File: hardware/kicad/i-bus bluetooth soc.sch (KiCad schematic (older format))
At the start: 35 parts, among them J1 CONN_3, J2 CONN_6, U1 CC2541, U2 TH8080, U3 MC34063, U4 TPS76933, X1 32 MHz

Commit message: Rules check found missing NCs
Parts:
- removed GND: GND, symbol GND
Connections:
- no-connect marks 2 -> 17
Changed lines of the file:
@@
-EESchema Schematic File Version 2  date Mon 17 Feb 2014 12:44:29 PM CST
+EESchema Schematic File Version 2  date Mon 17 Feb 2014 01:35:22 PM CST
 LIBS:power
 LIBS:device
@@
 LIBS:TLV70033
 LIBS:guan
-EELAYER 43  0
+LIBS:i-bus bluetooth soc-cache
+EELAYER 25  0
 EELAYER END
 $Descr A4 11700 8267
@@
 Comment4 ""
 $EndDescr
+NoConn ~ 8800 5000
+NoConn ~ 8800 4900
+NoConn ~ 8800 4800
+NoConn ~ 8800 4500
+NoConn ~ 8800 4400
+NoConn ~ 8800 3100
+NoConn ~ 8800 3000
+NoConn ~ 8800 2700
+NoConn ~ 8800 2600
+NoConn ~ 8800 2500
+NoConn ~ 8800 2400
+NoConn ~ 8800 2000
+NoConn ~ 8800 1900
+NoConn ~ 8800 1600
+NoConn ~ 8800 1500
 Text Label 3250 4850 0    60   ~ 0
 AVDD1,2,4
@@
 DVDD2
 $Comp
-L +3.3V #PWR?
+L +3.3V #+3.3V01
 U 1 1 530255BC
 P 1400 4800
-F 0 "#PWR?" H 1400 4760 30  0001 C CNN
+F 0 "#+3.3V01" H 1400 4760 30  0001 C CNN
 F 1 "+3.3V" H 1400 4910 30  0000 C CNN
 	1    1400 4800
@@
 $EndComp
 $Comp
-L GND #PWR?
+L GND #GND02
 U 1 1 53025587
 P 3600 5350
-F 0 "#PWR?" H 3600 5350 30  0001 C CNN
+F 0 "#GND02" H 3600 5350 30  0001 C CNN
 F 1 "GND" H 3600 5280 30  0001 C CNN
 	1    3600 5350
@@
 $EndComp
 $Comp
-L GND #PWR?
+L GND #GND03
 U 1 1 53025585
 P 3250 5350
-F 0 "#PWR?" H 3250 5350 30  0001 C CNN
+F 0 "#GND03" H 3250 5350 30  0001 C CNN
 F 1 "GND" H 3250 5280 30  0001 C CNN
 	1    3250 5350
@@
 $EndComp
 $Comp
-L GND #PWR?
+L GND #GND04
 U 1 1 53025583
 P 1500 5350
-F 0 "#PWR?" H 1500 5350 30  0001 C CNN
+F 0 "#GND04" H 1500 5350 30  0001 C CNN
 F 1 "GND" H 1500 5280 30  0001 C CNN
 	1    1500 5350
@@
 $EndComp
 $Comp
-L GND #PWR?
+L GND #GND05
 U 1 1 53025580
 P 2900 5350
-F 0 "#PWR?" H 2900 5350 30  0001 C CNN
+F 0 "#GND05" H 2900 5350 30  0001 C CNN
 F 1 "GND" H 2900 5280 30  0001 C CNN
 	1    2900 5350
@@
 $EndComp
 $Comp
-L GND #PWR?
+L GND #GND06
 U 1 1 5302557E
 P 2200 5350
-F 0 "#PWR?" H 2200 5350 30  0001 C CNN
+F 0 "#GND06" H 2200 5350 30  0001 C CNN
 F 1 "GND" H 2200 5280 30  0001 C CNN
 	1    2200 5350
@@
 $EndComp
 $Comp
-L GND #PWR?
+L GND #GND07
 U 1 1 5302557C
 P 2550 5350
-F 0 "#PWR?" H 2550 5350 30  0001 C CNN
+F 0 "#GND07" H 2550 5350 30  0001 C CNN
 F 1 "GND" H 2550 5280 30  0001 C CNN
 	1    2550 5350
@@
 $EndComp
 $Comp
-L GND #PWR?
+L GND #GND08
 U 1 1 53025577
 P 1850 5350
-F 0 "#PWR?" H 1850 5350 30  0001 C CNN
+F 0 "#GND08" H 1850 5350 30  0001 C CNN
 F 1 "GND" H 1850 5280 30  0001 C CNN
 	1    1850 5350
@@
 RESET
 $Comp
-L GND #PWR?
+L GND #GND09
 U 1 1 53025220
 P 7550 2450
-F 0 "#PWR?" H 7550 2450 30  0001 C CNN
+F 0 "#GND09" H 7550 2450 30  0001 C CNN
 F 1 "GND" H 7550 2380 30  0001 C CNN
 	1    7550 2450
@@
 $EndComp
 $Comp
-L GND #PWR?
+L GND #GND010
 U 1 1 5302478B
 P 8400 2650
-F 0 "#PWR?" H 8400 2650 30  0001 C CNN
+F 0 "#GND010" H 8400 2650 30  0001 C CNN
 F 1 "GND" H 8400 2580 30  0001 C CNN
 	1    8400 2650
@@
 $EndComp
 $Comp
-L GND #PWR?
+L GND #GND011
 U 1 1 53019952
 P 7850 4350
-F 0 "#PWR?" H 7850 4350 30  0001 C CNN
+F 0 "#GND011" H 7850 4350 30  0001 C CNN
 F 1 "GND" H 7850 4280 30  0001 C CNN
 	1    7850 4350
@@
 $EndComp
 $Comp
-L GND #PWR?
+L GND #GND012
 U 1 1 5301988F
 P 8750 5750
-F 0 "#PWR?" H 8750 5750 30  0001 C CNN
+F 0 "#GND012" H 8750 5750 30  0001 C CNN
 F 1 "GND" H 8750 5680 30  0001 C CNN
 	1    8750 5750
@@
 $EndComp
 $Comp
-L GND #PWR?
+L GND #GND013
 U 1 1 5301985C
 P 8700 1350
-F 0 "#PWR?" H 8700 1350 30  0001 C CNN
+F 0 "#GND013" H 8700 1350 30  0001 C CNN
 F 1 "GND" H 8700 1280 30  0001 C CNN
 	1    8700 1350
@@
 $EndComp
 $Comp
-L +3.3V #PWR?
+L +3.3V #+3.3V014
 U 1 1 53019827
 P 8700 2000
-F 0 "#PWR?" H 8700 1960 30  0001 C CNN
+F 0 "#+3.3V014" H 8700 1960 30  0001 C CNN
 F 1 "+3.3V" H 8700 2110 30  0000 C CNN
 	1    8700 2000
@@
 $EndComp
 $Comp
-L GND #PWR?
+L GND #GND015
 U 1 1 5301977F
 P 2400 4150
-F 0 "#PWR?" H 2400 4150 30  0001 C CNN
+F 0 "#GND015" H 2400 4150 30  0001 C CNN
 F 1 "GND" H 2400 4080 30  0001 C CNN
 	1    2400 4150
@@
 $EndComp
 $Comp
-L +3.3V #PWR?
+L +3.3V #+3.3V016
 U 1 1 53019764
 P 3100 3550
-F 0 "#PWR?" H 3100 3510 30  0001 C CNN
+F 0 "#+3.3V016" H 3100 3510 30  0001 C CNN
 F 1 "+3.3V" H 3100 3660 30  0000 C CNN
 	1    3100 3550
@@
 $EndComp
 $Comp
-L +5V #PWR?
+L +5V #+5V017
 U 1 1 5301973E
 P 1900 3550
-F 0 "#PWR?" H 1900 3640 20  0001 C CNN
+F 0 "#+5V017" H 1900 3640 20  0001 C CNN
 F 1 "+5V" H 1900 3640 30  0000 C CNN
 	1    1900 3550
@@
 $EndComp
 $Comp
-L +5V #PWR?
+L +5V #+5V018
 U 1 1 53019726
 P 3850 1250
-F 0 "#PWR?" H 3850 1340 20  0001 C CNN
+F 0 "#+5V018" H 3850 1340 20  0001 C CNN
 F 1 "+5V" H 3850 1340 30  0000 C CNN
 	1    3850 1250
@@
 $EndComp
 $Comp
-L +5V #PWR?
+L +5V #+5V019
 U 1 1 530196FF
 P 8450 1550
-F 0 "#PWR?" H 8450 1640 20  0001 C CNN
+F 0 "#+5V019" H 8450 1640 20  0001 C CNN
 F 1 "+5V" H 8450 1640 30  0000 C CNN
 	1    8450 1550
@@
 $EndComp
 $Comp
-L GND #PWR?
+L GND #GND020
 U 1 1 53018A16
 P 2450 2800
-F 0 "#PWR?" H 2450 2800 30  0001 C CNN
+F 0 "#GND020" H 2450 2800 30  0001 C CNN
 F 1 "GND" H 2450 2730 30  0001 C CNN
 	1    2450 2800
@@
 $EndComp
 $Comp
-L +BATT #PWR?
+L +BATT #+BATT021
 U 1 1 53010E72
 P 2450 1150
-F 0 "#PWR?" H 2450 1100 20  0001 C CNN
+F 0 "#+BATT021" H 2450 1100 20  0001 C CNN
 F 1 "+BATT" H 2450 1250 30  0000 C CNN
 	1    2450 1150
@@
 $EndComp
 $Comp
-L +BATT #PWR?
+L +BATT #+BATT022
 U 1 1 53010DF8
 P 6550 1500
-F 0 "#PWR?" H 6550 1450 20  0001 C CNN
+F 0 "#+BATT022" H 6550 1450 20  0001 C CNN
 F 1 "+BATT" H 6550 1600 30  0000 C CNN
 	1    6550 1500
@@
 $EndComp
 $Comp
-L GND GND
+L GND #GND023
 U 1 1 5300FA2A
 P 6550 1900
-F 0 "GND" H 6550 1900 30  0001 C CNN
+F 0 "#GND023" H 6550 1900 30  0001 C CNN
 F 1 "GND" H 6550 1830 30  0001 C CNN
 	1    6550 1900

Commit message: New version using the MCP2025
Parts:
- removed C2: 100 uF, symbol CP1
- removed C3: 470 pF, symbol C
- removed C4: 1 uF, symbol C
- removed D1: DIODE, symbol DIODE
- removed L1: INDUCTOR, symbol INDUCTOR
- removed R2: 0.22, symbol R
- removed R3: 4.7 K, symbol R
- removed R4: 1.5 K, symbol R
- removed U2: TH8080, MODULE, symbol TH8080
- removed U3: MC34063, symbol MC34063
- removed U4: TPS76933, symbol TPS769XX
- added C2: 10 uF, symbol C
- added U1: MCP2025, MODULE, symbol MCP2025
- C1: value 22 uF -> 100 uF
- renumbered C12 to C10, C13 to C11, C14 to C12, C15 to C13, C7 to C3, C6 to C4, C8 to C5, C5 to C6, C9 to C7, C10 to C8, C11 to C9, D2 to D1, D3 to D2, R5 to R1, R6 to R2, R1 to R3, U1 to U2
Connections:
- net labels added: CS, RX-0, RX-1, TX-0, TX-1
- net labels removed: +5V, +BATT, RX0, TX0
- wire segments 129 -> 94
- no-connect marks 17 -> 15
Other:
- moved on the sheet: A1, C10, C11, C12, C13, C3, C4, C5, C6, C7, C8, C9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

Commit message: Component placement, fixed some modules
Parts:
- C1: value 100 uF -> 47 uF
- C2: value 10 uF -> 4.7 uF
- X1: symbol CRYSTAL -> FA-128
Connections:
- wire segments 94 -> 96
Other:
- moved on the sheet: C3, C4
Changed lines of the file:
@@
-EESchema Schematic File Version 2  date Wed 19 Feb 2014 11:02:51 PM CST
+EESchema Schematic File Version 2  date Thu 20 Feb 2014 11:27:15 PM CST
 LIBS:power
 LIBS:device
@@
 Sheet 1 1
 Title ""
-Date "20 feb 2014"
+Date "21 feb 2014"
 Rev ""
 Comp ""
@@
 Comment4 ""
 $EndDescr
+Connection ~ 6850 3800
+Wire Wire Line
+	6850 3800 6850 3400
 Wire Wire Line
 	2250 1150 2250 1100
@@
 Connection ~ 7050 6100
 Wire Wire Line
-	7050 6100 7050 6150
+	7050 6150 7050 6100
 Connection ~ 7750 6100
 Wire Wire Line
@@
 	8000 5150 8000 5200
 Wire Wire Line
-	6600 3750 6600 3800
-Connection ~ 6600 3200
-Wire Wire Line
-	6650 3200 6600 3200
-Wire Wire Line
-	7300 3350 7300 3000
+	6550 3800 6550 3750
+Connection ~ 6550 3200
+Wire Wire Line
+	6700 3200 6550 3200
+Wire Wire Line
+	7350 3350 7350 3000
 Wire Wire Line
 	8200 4750 8200 4700
@@
 	8200 5150 8200 5250
 Wire Wire Line
-	7300 3000 8250 3000
-Wire Wire Line
-	8250 2900 6600 2900
-Wire Wire Line
-	6600 2900 6600 3350
-Wire Wire Line
-	7250 3200 7300 3200
-Connection ~ 7300 3200
-Wire Wire Line
-	7300 3850 7300 3750
-Connection ~ 7300 3800
+	7350 3000 8250 3000
+Wire Wire Line
+	8250 2900 6550 2900
+Wire Wire Line
+	6550 2900 6550 3350
+Wire Wire Line
+	7300 3200 7350 3200
+Connection ~ 7350 3200
+Wire Wire Line
+	7350 3850 7350 3750
+Connection ~ 7350 3800
 Wire Wire Line
 	8250 3700 8000 3700
@@
 Wire Wire Line
 	6150 3800 6150 3750
-Connection ~ 6600 3800
-Wire Wire Line
-	7300 3800 5750 3800
+Connection ~ 6550 3800
+Wire Wire Line
+	7350 3800 5750 3800
 Wire Wire Line
 	5750 3800 5750 3750
@@
 Connection ~ 8450 6100
 Wire Wire Line
-	8800 6150 8800 6100
+	8800 6100 8800 6150
 Connection ~ 8800 6100
 Wire Wire Line
@@
 Wire Wire Line
 	2350 1900 2400 1900
+Wire Wire Line
+	7150 3400 7150 3800
+Connection ~ 7150 3800
 $Comp
 L GND #PWR01
@@
 P 2250 1350
 F 0 "C1" H 2300 1450 50  0000 L CNN
-F 1 "100 uF" H 2300 1250 50  0000 L CNN
+F 1 "47 uF" H 2300 1250 50  0000 L CNN
 	1    2250 1350
 	1    0    0    -1
@@
 P 4500 1850
 F 0 "C2" H 4550 1950 50  0000 L CNN
-F 1 "10 uF" H 4550 1750 50  0000 L CNN
+F 1 "4.7 uF" H 4550 1750 50  0000 L CNN
 	1    4500 1850
 	1    0    0    -1
@@
 L C C4
 U 1 1 53019A14
-P 7300 3550
-F 0 "C4" H 7350 3650 50  0000 L CNN
-F 1 "12 pF" H 7350 3450 50  0000 L CNN
-	1    7300 3550
+P 7350 3550
+F 0 "C4" H 7400 3650 50  0000 L CNN
+F 1 "12 pF" H 7400 3450 50  0000 L CNN
+	1    7350 3550
 	1    0    0    -1
 $EndComp
@@
 L C C3
 U 1 1 53019A10
-P 6600 3550
-F 0 "C3" H 6650 3650 50  0000 L CNN
-F 1 "12 pF" H 6650 3450 50  0000 L CNN
-	1    6600 3550
-	1    0    0    -1
-$EndComp
-$Comp
-L CRYSTAL X1
+P 6550 3550
+F 0 "C3" H 6600 3650 50  0000 L CNN
+F 1 "12 pF" H 6600 3450 50  0000 L CNN
+	1    6550 3550
+	1    0    0    -1
+$EndComp
+$Comp
+L FA-128 X1
 U 1 1 530199D3
-P 6950 3200
-F 0 "X1" H 6950 3350 60  0000 C CNN
-F 1 "32 MHz" H 6950 3050 60  0000 C CNN
-F 4 "FA-128 32.0000MF20X-K3" H 6950 3200 60  0001 C CNN "PN"
-	1    6950 3200
-	1    0    0    -1
+P 7000 3200
+F 0 "X1" H 7000 2950 60  0000 C CNN
+F 1 "32 MHz" H 7000 3400 60  0000 C CNN
+F 4 "FA-128 32.0000MF20X-K3" H 7000 3200 60  0001 C CNN "PN"
+	1    7000 3200
+	-1   0    0    -1
 $EndComp
 $Comp
 L GND #GND014
 U 1 1 53019952
-P 7300 3850
-F 0 "#GND014" H 7300 3850 30  0001 C CNN
-F 1 "GND" H 7300 3780 30  0001 C CNN
-	1    7300 3850
+P 7350 3850
+F 0 "#GND014" H 7350 3850 30  0001 C CNN
+F 1 "GND" H 7350 3780 30  0001 C CNN
+	1    7350 3850
 	1    0    0    -1
 $EndComp
@@
 $EndComp
 $Comp
-L +3.3V #+3.3V017
+L +3.3V #+017
 U 1 1 53019827
 P 8150 1350
-F 0 "#+3.3V017" H 8150 1310 30  0001 C CNN
+F 0 "#+017" H 8150 1310 30  0001 C CNN
 F 1 "+3.3V" H 8150 1460 30  0000 C CNN
 	1    8150 1350

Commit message: Changed power supply caps.
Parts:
- C1: value 47 uF -> 100 uF; symbol C -> CP1
- C2: value 4.7 uF -> 10 uF
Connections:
- net GND: now also C1.2; no longer C1.1
- net at J1.3 (P3), U1.1 (VBB): now also C1.1; no longer C1.2
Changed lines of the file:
@@
-EESchema Schematic File Version 2  date Thu 20 Feb 2014 11:27:15 PM CST
+EESchema Schematic File Version 2  date Fri 21 Feb 2014 09:56:01 PM CST
 LIBS:power
 LIBS:device
@@
 Sheet 1 1
 Title ""
-Date "21 feb 2014"
+Date "22 feb 2014"
 Rev ""
 Comp ""
@@
 $EndComp
 $Comp
-L C C1
+L CP1 C1
 U 1 1 530588C6
 P 2250 1350
 F 0 "C1" H 2300 1450 50  0000 L CNN
-F 1 "47 uF" H 2300 1250 50  0000 L CNN
+F 1 "100 uF" H 2300 1250 50  0000 L CNN
 	1    2250 1350
-	1    0    0    -1
+	1    0    0    1
 $EndComp
 $Comp
@@
 P 4500 1850
 F 0 "C2" H 4550 1950 50  0000 L CNN
-F 1 "4.7 uF" H 4550 1750 50  0000 L CNN
+F 1 "10 uF" H 4550 1750 50  0000 L CNN
 	1    4500 1850
 	1    0    0    -1

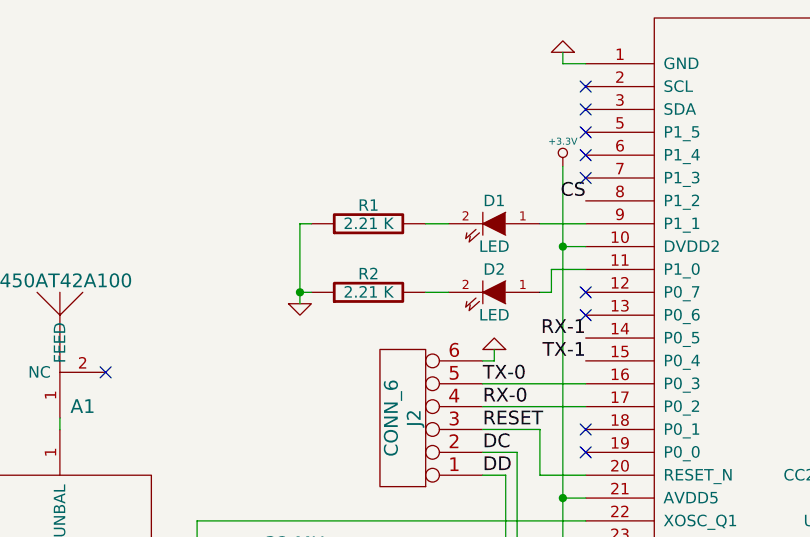
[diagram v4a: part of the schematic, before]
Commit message: Changed the LEDs to active-low
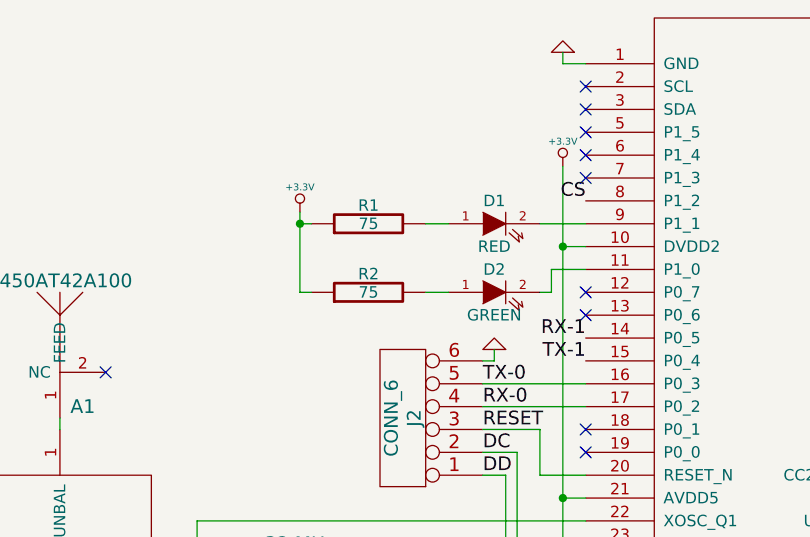
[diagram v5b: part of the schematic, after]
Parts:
- D1: value LED -> RED
- D2: value LED -> GREEN
- R1, R2: value 2.21 K -> 75
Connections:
- net +3.3V: now also R1.1, R2.1
- net GND: no longer R1.1, R2.1
- net at U2.11 (P1_0): now also D2.2 (K); no longer D2.1 (A)
- net at U2.9 (P1_1): now also D1.2 (K); no longer D1.1 (A)
- net at R1.2: now also D1.1 (A); no longer D1.2 (K)
- net at R2.2: now also D2.1 (A); no longer D2.2 (K)
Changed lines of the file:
@@
-EESchema Schematic File Version 2  date Fri 21 Feb 2014 09:56:01 PM CST
+EESchema Schematic File Version 2
 LIBS:power
 LIBS:device
@@
 LIBS:MCP2025
 LIBS:i-bus bluetooth soc-cache
-EELAYER 25  0
+EELAYER 27 0
 EELAYER END
-$Descr A4 11700 8267
+$Descr A4 11693 8268
 encoding utf-8
 Sheet 1 1
 Title ""
-Date "22 feb 2014"
+Date "23 feb 2014"
 Rev ""
 Comp ""
@@
 Wire Wire Line
 	7550 1600 7650 1600
-Connection ~ 7000 1900
-Wire Wire Line
-	7050 1900 7000 1900
+Wire Wire Line
+	7000 1900 7050 1900
 Wire Wire Line
 	8250 1800 8100 1800
@@
 Wire Wire Line
 	7050 1600 7000 1600
-Wire Wire Line
-	7000 1600 7000 1950
 Wire Wire Line
 	7650 1900 7550 1900
@@
 F 0 "#PWR01" H 2250 1100 30  0001 C CNN
 F 1 "GND" H 2250 1030 30  0001 C CNN
+F 2 "" H 2250 1100 60  0001 C CNN
+F 3 "" H 2250 1100 60  0001 C CNN
 	1    2250 1100
 	-1   0    0    1
@@
 F 0 "C1" H 2300 1450 50  0000 L CNN
 F 1 "100 uF" H 2300 1250 50  0000 L CNN
+F 2 "" H 2250 1350 60  0001 C CNN
+F 3 "" H 2250 1350 60  0001 C CNN
 	1    2250 1350
 	1    0    0    1
@@
 F 0 "#PWR02" H 4500 2100 30  0001 C CNN
 F 1 "GND" H 4500 2030 30  0001 C CNN
+F 2 "" H 4500 2100 60  0001 C CNN
+F 3 "" H 4500 2100 60  0001 C CNN
 	1    4500 2100
 	1    0    0    -1
@@
 F 0 "C2" H 4550 1950 50  0000 L CNN
 F 1 "10 uF" H 4550 1750 50  0000 L CNN
+F 2 "" H 4500 1850 60  0001 C CNN
+F 3 "" H 4500 1850 60  0001 C CNN
 	1    4500 1850
 	1    0    0    -1
@@
 F 0 "#PWR03" H 4500 1460 30  0001 C CNN
 F 1 "+3.3V" H 4500 1610 30  0000 C CNN
+F 2 "" H 4500 1500 60  0001 C CNN
+F 3 "" H 4500 1500 60  0001 C CNN
 	1    4500 1500
 	1    0    0    -1
@@
 F 0 "#+04" H 6950 6010 30  0001 C CNN
 F 1 "+3.3V" H 6950 6160 30  0000 C CNN
+F 2 "" H 6950 6050 60  0001 C CNN
+F 3 "" H 6950 6050 60  0001 C CNN
 	1    6950 6050
 	1    0    0    -1
@@
 F 0 "#GND05" H 9150 6600 30  0001 C CNN
 F 1 "GND" H 9150 6530 30  0001 C CNN
+F 2 "" H 9150 6600 60  0001 C CNN
+F 3 "" H 9150 6600 60  0001 C CNN
 	1    9150 6600
 	1    0    0    -1
@@
 F 0 "#GND06" H 8800 6600 30  0001 C CNN
 F 1 "GND" H 8800 6530 30  0001 C CNN
+F 2 "" H 8800 6600 60  0001 C CNN
+F 3 "" H 8800 6600 60  0001 C CNN
 	1    8800 6600
 	1    0    0    -1
@@
 F 0 "#GND07" H 7050 6600 30  0001 C CNN
 F 1 "GND" H 7050 6530 30  0001 C CNN
+F 2 "" H 7050 6600 60  0001 C CNN
+F 3 "" H 7050 6600 60  0001 C CNN
 	1    7050 6600
 	1    0    0    -1
@@
 F 0 "#GND08" H 8450 6600 30  0001 C CNN
 F 1 "GND" H 8450 6530 30  0001 C CNN
+F 2 "" H 8450 6600 60  0001 C CNN
+F 3 "" H 8450 6600 60  0001 C CNN
 	1    8450 6600
 	1    0    0    -1
@@
 F 0 "#GND09" H 7750 6600 30  0001 C CNN
 F 1 "GND" H 7750 6530 30  0001 C CNN
+F 2 "" H 7750 6600 60  0001 C CNN
+F 3 "" H 7750 6600 60  0001 C CNN
 	1    7750 6600
 	1    0    0    -1
@@
 F 0 "#GND010" H 8100 6600 30  0001 C CNN
 F 1 "GND" H 8100 6530 30  0001 C CNN
+F 2 "" H 8100 6600 60  0001 C CNN
+F 3 "" H 8100 6600 60  0001 C CNN
 	1    8100 6600
 	1    0    0    -1
@@
 F 0 "#GND011" H 7400 6600 30  0001 C CNN
 F 1 "GND" H 7400 6530 30  0001 C CNN
+F 2 "" H 7400 6600 60  0001 C CNN
+F 3 "" H 7400 6600 60  0001 C CNN
 	1    7400 6600
 	1    0    0    -1
@@
 F 0 "C13" H 9200 6450 50  0000 L CNN
 F 1 "220 pF" H 9200 6250 50  0000 L CNN
+F 2 "" H 9150 6350 60  0001 C CNN
+F 3 "" H 9150 6350 60  0001 C CNN
 	1    9150 6350
 	1    0    0    -1
@@
 F 0 "C12" H 8850 6450 50  0000 L CNN
 F 1 "100 nF" H 8850 6250 50  0000 L CNN
+F 2 "" H 8800 6350 60  0001 C CNN
+F 3 "" H 8800 6350 60  0001 C CNN
 	1    8800 6350
 	1    0    0    -1
@@
 F 0 "C7" H 7100 6450 50  0000 L CNN
 F 1 "1 uF" H 7100 6250 50  0000 L CNN
+F 2 "" H 7050 6350 60  0001 C CNN
+F 3 "" H 7050 6350 60  0001 C CNN
 	1    7050 6350
 	1    0    0    -1
@@
 F 0 "C11" H 8500 6450 50  0000 L CNN
 F 1 "100 nF" H 8500 6250 50  0000 L CNN
+F 2 "" H 8450 6350 60  0001 C CNN
+F 3 "" H 8450 6350 60  0001 C CNN
 	1    8450 6350
 	1    0    0    -1
@@
 F 0 "C9" H 7800 6450 50  0000 L CNN
 F 1 "100 nF" H 7800 6250 50  0000 L CNN
+F 2 "" H 7750 6350 60  0001 C CNN
+F 3 "" H 7750 6350 60  0001 C CNN
 	1    7750 6350
 	1    0    0    -1
@@
 F 0 "C10" H 8150 6450 50  0000 L CNN
 F 1 "100 nF" H 8150 6250 50  0000 L CNN
+F 2 "" H 8100 6350 60  0001 C CNN
+F 3 "" H 8100 6350 60  0001 C CNN
 	1    8100 6350
 	1    0    0    -1
@@
 F 0 "C8" H 7450 6450 50  0000 L CNN
 F 1 "100 nF" H 7450 6250 50  0000 L CNN
+F 2 "" H 7400 6350 60  0001 C CNN
+F 3 "" H 7400 6350 60  0001 C CNN
 	1    7400 6350
 	1    0    0    -1
@@
 F 0 "C5" H 7600 5050 50  0000 L CNN
 F 1 "1000 pF" H 7600 4850 50  0000 L CNN
+F 2 "" H 7550 4950 60  0001 C CNN
+F 3 "" H 7550 4950 60  0001 C CNN
 	1    7550 4950
 	1    0    0    -1
@@
 Text Label 7800 2500 0    60   ~ 0
 RESET
-$Comp
-L GND #GND012
-U 1 1 53025220
-P 7000 1950
-F 0 "#GND012" H 7000 1950 30  0001 C CNN
-F 1 "GND" H 7000 1880 30  0001 C CNN
-	1    7000 1950
-	1    0    0    -1
-$EndComp
 $Comp
 L R R2
@@
 P 7300 1900
 F 0 "R2" V 7380 1900 50  0000 C CNN
-F 1 "2.21 K" V 7300 1900 50  0000 C CNN
+F 1 "75" V 7300 1900 50  0000 C CNN
+F 2 "" H 7300 1900 60  0001 C CNN
+F 3 "" H 7300 1900 60  0001 C CNN
 	1    7300 1900
 	0    -1   -1   0
@@
 P 7300 1600
 F 0 "R1" V 7380 1600 50  0000 C CNN
-F 1 "2.21 K" V 7300 1600 50  0000 C CNN
+F 1 "75" V 7300 1600 50  0000 C CNN
+F 2 "" H 7300 1600 60  0001 C CNN
+F 3 "" H 7300 1600 60  0001 C CNN
 	1    7300 1600
 	0    -1   -1   0
@@
 P 7850 1900
 F 0 "D2" H 7850 2000 50  0000 C CNN
-F 1 "LED" H 7850 1800 50  0000 C CNN
+F 1 "GREEN" H 7850 1800 50  0000 C CNN
+F 2 "" H 7850 1900 60  0001 C CNN
+F 3 "" H 7850 1900 60  0001 C CNN
 	1    7850 1900
-	-1   0    0    -1
+	1    0    0    -1
 $EndComp
 $Comp
@@
 P 7850 1600
 F 0 "D1" H 7850 1700 50  0000 C CNN
-F 1 "LED" H 7850 1500 50  0000 C CNN
+F 1 "RED" H 7850 1500 50  0000 C CNN
+F 2 "" H 7850 1600 60  0001 C CNN
+F 3 "" H 7850 1600 60  0001 C CNN
 	1    7850 1600
-	-1   0    0    -1
+	1    0    0    -1
 $EndComp
 $Comp
@@
 F 0 "J2" V 7400 2450 60  0000 C CNN
 F 1 "CONN_6" V 7500 2450 60  0000 C CNN
+F 2 "" H 7450 2450 60  0001 C CNN
+F 3 "" H 7450 2450 60  0001 C CNN
 	1    7450 2450
 	-1   0    0    1
@@
 F 0 "#GND013" H 7850 2150 30  0001 C CNN
 F 1 "GND" H 7850 2080 30  0001 C CNN
+F 2 "" H 7850 2150 60  0001 C CNN
+F 3 "" H 7850 2150 60  0001 C CNN
 	1    7850 2150
 	-1   0    0    1
@@
 F 0 "A1" H 6050 2100 60  0000 C CNN
 F 1 "2450AT42A100" H 5950 2650 60  0000 C CNN
+F 2 "" H 5950 2250 60  0001 C CNN
+F 3 "" H 5950 2250 60  0001 C CNN
 	1    5950 2250
 	1    0    0    -1
@@
 F 0 "FL1" H 5950 3100 60  0000 C CNN
 F 1 "2450BM15A0002" H 6000 2400 60  0000 C CNN
+F 2 "" H 5950 3150 60  0001 C CNN
+F 3 "" H 5950 3150 60  0001 C CNN
 	1    5950 3150
 	1    0    0    -1
@@
 F 0 "C4" H 7400 3650 50  0000 L CNN
 F 1 "12 pF" H 7400 3450 50  0000 L CNN
+F 2 "" H 7350 3550 60  0001 C CNN
+F 3 "" H 7350 3550 60  0001 C CNN
 	1    7350 3550
 	1    0    0    -1
@@
 F 0 "C3" H 6600 3650 50  0000 L CNN
 F 1 "12 pF" H 6600 3450 50  0000 L CNN
+F 2 "" H 6550 3550 60  0001 C CNN
+F 3 "" H 6550 3550 60  0001 C CNN
 	1    6550 3550
 	1    0    0    -1
@@
 F 0 "X1" H 7000 2950 60  0000 C CNN
 F 1 "32 MHz" H 7000 3400 60  0000 C CNN
+F 2 "" H 7000 3200 60  0001 C CNN
+F 3 "" H 7000 3200 60  0001 C CNN
 F 4 "FA-128 32.0000MF20X-K3" H 7000 3200 60  0001 C CNN "PN"
 	1    7000 3200
@@
 F 0 "#GND014" H 7350 3850 30  0001 C CNN
 F 1 "GND" H 7350 3780 30  0001 C CNN
+F 2 "" H 7350 3850 60  0001 C CNN
+F 3 "" H 7350 3850 60  0001 C CNN
 	1    7350 3850
 	1    0    0    -1
@@
 F 0 "R3" V 8080 4900 50  0000 C CNN
 F 1 "56 K 1%" V 8000 4900 50  0000 C CNN
+F 2 "" H 8000 4900 60  0001 C CNN
+F 3 "" H 8000 4900 60  0001 C CNN
 	1    8000 4900
 	-1   0    0    1
@@
 F 0 "#GND015" H 8200 5250 30  0001 C CNN
 F 1 "GND" H 8200 5180 30  0001 C CNN
+F 2 "" H 8200 5250 60  0001 C CNN
+F 3 "" H 8200 5250 60  0001 C CNN
 	1    8200 5250
 	1    0    0    -1
@@
 F 0 "C6" H 8250 5050 50  0000 L CNN
 F 1 "1 uF" H 8250 4850 50  0000 L CNN
+F 2 "" H 8200 4950 60  0001 C CNN
+F 3 "" H 8200 4950 60  0001 C CNN
 	1    8200 4950
 	1    0    0    -1
@@
 F 0 "#GND016" H 8150 850 30  0001 C CNN
 F 1 "GND" H 8150 780 30  0001 C CNN
+F 2 "" H 8150 850 60  0001 C CNN
+F 3 "" H 8150 850 60  0001 C CNN
 	1    8150 850
 	-1   0    0    1
@@
 F 0 "#+017" H 8150 1310 30  0001 C CNN
 F 1 "+3.3V" H 8150 1460 30  0000 C CNN
+F 2 "" H 8150 1350 60  0001 C CNN
+F 3 "" H 8150 1350 60  0001 C CNN
 	1    8150 1350
 	1    0    0    -1
@@
 F 0 "#GND018" H 2250 1850 30  0001 C CNN
 F 1 "GND" H 2250 1780 30  0001 C CNN
+F 2 "" H 2250 1850 60  0001 C CNN
+F 3 "" H 2250 1850 60  0001 C CNN
 	1    2250 1850
 	1    0    0    -1
@@
 F 0 "J1" V 1700 1700 50  0000 C CNN
 F 1 "CONN_3" V 1800 1700 40  0000 C CNN
+F 2 "" H 1750 1700 60  0001 C CNN
+F 3 "" H 1750 1700 60  0001 C CNN
 	1    1750 1700
 	-1   0    0    1
 $EndComp
+$Comp
+L +3.3V #PWR?
+U 1 1 53094526
+P 7000 1550
+F 0 "#PWR?" H 7000 1510 30  0001 C CNN
+F 1 "+3.3V" H 7000 1660 30  0000 C CNN
+F 2 "" H 7000 1550 60  0000 C CNN
+F 3 "" H 7000 1550 60  0000 C CNN
+	1    7000 1550
+	1    0    0    -1
+$EndComp
+Wire Wire Line
+	7000 1550 7000 1900
+Connection ~ 7000 1600
 $EndSCHEMATC
